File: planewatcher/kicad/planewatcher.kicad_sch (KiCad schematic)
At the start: 14 parts, among them J2 RF_IN, J3 BMI-S-209-F, J4 FPGA BANK 33, J5 FPGA BANK 35 V1.2/V1.3, J6 GPS _IN

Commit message: review & consolidate all capacitors
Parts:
- C1: Design Notes (none) -> ~18µF after DC bias de-rating; MPN CL31A226KOHNNNE -> GCJ31CR71A226KE01K; Manufacturer Samsung -> Murata Electronics; Package 1206 -> 1206 (3216 Metric); Suggested Part Samsung CL31A226KOHNNNE -> (none)
- C2: MPN GRM155R71H104KE14D -> GCM155R71A104KA55D; Manufacturer Murata -> Murata Electronics; Package 1206 -> 0402 (1005 Metric); Suggested Part Murata GRM155R71H104KE14D -> (none)
- C3: MPN GRM1555C1H102JA01D -> GRM1555C1H102FA01D; Manufacturer Murata -> Murata Electronics; Package 0402 -> 0402 (1005 Metric); Suggested Part Murata GRM1555C1H102JA01D -> (none)
- FL1, FL2: Suggested Part Tai-Saw TA2003A -> (none)
- J2: Suggested Part Amphenol RF 132289 -> (none)
- J3: Suggested Part Laird/BMI BMI-S-209-F -> (none)
- J4, J5: Suggested Part Samtec TSW-120-07-L-D -> (none)
- J6: Purpose Accepts the external 1090MHz antenna input. -> Accepts the external GPS/GNSS antenna input.; Suggested Part Amphenol RF 132289 -> (none)
- L1: Suggested Part Würth Elektronik 74269262601 -> (none)
- R1: Suggested Part Yageo RC0402FR-0710KL -> (none)
- R2: Suggested Part Yageo RC0402FR-07330RL -> (none)
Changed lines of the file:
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@@
 			)
 		)
-		(property "Suggested Part" "Samtec TSW-120-07-L-D"
+		(property "Purpose" "Breaks out FPGA bank 35 I/O and power pins to the carrier/FPGA interface."
 			(at 106.68 168.91 0)
 			(hide yes)
@@
 			)
 		)
-		(property "Purpose" "Breaks out FPGA bank 35 I/O and power pins to the carrier/FPGA interface."
+		(property "Notes" ""
 			(at 106.68 168.91 0)
 			(hide yes)
@@
 			)
 		)
-		(property "Notes" ""
+		(property "Mount_Type" ""
 			(at 106.68 168.91 0)
 			(hide yes)
@@
 			)
 		)
-		(property "Suggested Part" "Yageo RC0402FR-07330RL"
+		(property "Purpose" "Series resistor between LT3045 power-good output and the FPGA monitor input."
 			(at 184.15 36.83 0)
 			(hide yes)
@@
 			)
 		)
-		(property "Purpose" "Series resistor between LT3045 power-good output and the FPGA monitor input."
+		(property "Mount_Type" ""
 			(at 184.15 36.83 0)
 			(hide yes)
@@
 			)
 		)
-		(property "Datasheet" ""
+		(property "Datasheet" "https://pim.murata.com/en-sg/pim/details/?partNum=GCJ31CR71A226KE01%23&displayChangeClass=productDetailPrint"
 			(at 120.65 38.1 0)
 			(hide yes)
@@
 			)
 		)
-		(property "Description" "22µF, X5R, ±10%, 16V, 1206 MLCC"
+		(property "Description" "22 µF ±10% 10V Ceramic Capacitor X7R 1206 (3216 Metric)"
 			(at 120.65 38.1 0)
 			(hide yes)
@@
 			)
 		)
-		(property "Package" "1206"
+		(property "Package" "1206 (3216 Metric)"
 			(at 120.65 38.1 0)
 			(hide yes)
@@
 			)
 		)
-		(property "MPN" "CL31A226KOHNNNE"
+		(property "MPN" "GCJ31CR71A226KE01K"
 			(at 120.65 38.1 0)
 			(hide yes)
@@
 			)
 		)
-		(property "Manufacturer" "Samsung"
+		(property "Manufacturer" "Murata Electronics"
 			(at 120.65 38.1 0)
 			(hide yes)
@@
 			)
 		)
-		(property "Suggested Part" "Samsung CL31A226KOHNNNE"
+		(property "Purpose" "Load-side bulk decoupling for the filtered 3V3A analog rail."
 			(at 120.65 38.1 0)
 			(hide yes)
@@
 			)
 		)
-		(property "Purpose" "Load-side bulk decoupling for the filtered 3V3A analog rail."
+		(property "Design Notes" "~18µF after DC bias de-rating"
+			(at 120.65 38.1 0)
+			(hide yes)
+			(show_name no)
+			(do_not_autoplace no)
+			(effects
+				(font
+					(size 1.27 1.27)
+				)
+			)
+		)
+		(property "Mount_Type" ""
 			(at 120.65 38.1 0)
 			(hide yes)
@@
 			)
 		)
-		(property "Datasheet" ""
+		(property "Datasheet" "https://search.murata.co.jp/Ceramy/image/img/A01X/G101/ENG/GCM155R71A104KA55-01.pdf"
 			(at 133.35 38.1 0)
 			(hide yes)
@@
 			)
 		)
-		(property "Description" "100nF, X7R, ±10%, 50V, 0402 MLCC"
+		(property "Description" "0.1 µF ±10% 10V Ceramic Capacitor X7R 0402 (1005 Metric)"
 			(at 133.35 38.1 0)
 			(hide yes)
@@
 			)
 		)
-		(property "Package" "1206"
+		(property "Package" "0402 (1005 Metric)"
 			(at 133.35 38.1 0)
 			(hide yes)
@@
 			)
 		)
-		(property "MPN" "GRM155R71H104KE14D"
+		(property "MPN" "GCM155R71A104KA55D"
 			(at 133.35 38.1 0)
 			(hide yes)
@@
 			)
 		)
-		(property "Manufacturer" "Murata"
+		(property "Manufacturer" "Murata Electronics"
 			(at 133.35 38.1 0)
 			(hide yes)
@@
 			)
 		)
-		(property "Suggested Part" "Murata GRM155R71H104KE14D"
+		(property "Purpose" "Load-side high-frequency decoupling for the filtered 3V3A analog rail."
 			(at 133.35 38.1 0)
 			(hide yes)
@@
 			)
 		)
-		(property "Purpose" "Load-side high-frequency decoupling for the filtered 3V3A analog rail."
+		(property "Mount_Type" ""
 			(at 133.35 38.1 0)
 			(hide yes)
@@
 			)
 		)
-		(property "Suggested Part" "Yageo RC0402FR-0710KL"
+		(property "Purpose" "Pulls the LT3045 open-collector power-good output up to 3V3."
 			(at 184.15 29.21 0)
 			(hide yes)
@@
 			)
 		)
-		(property "Purpose" "Pulls the LT3045 open-collector power-good output up to 3V3."
+		(property "Mount_Type" ""
 			(at 184.15 29.21 0)
 			(hide yes)
@@
 			)
 		)
+		(property "Mount_Type" ""
+			(at 127 34.29 0)
+			(hide yes)
+			(show_name no)
+			(do_not_autoplace no)
+			(effects
+				(font
+					(size 1.27 1.27)
+				)
+			)
+		)
 		(pin "1"
 		)
@@
 			)
 		)
-		(property "Suggested Part" "Tai-Saw TA2003A"
+		(property "Purpose" "Band-limits the ADS-B 1090MHz RF path and rejects out-of-band energy."
 			(at 96.52 77.47 0)
 			(hide yes)
@@
 			)
 		)
-		(property "Purpose" "Band-limits the ADS-B 1090MHz RF path and rejects out-of-band energy."
+		(property "Notes" ""
 			(at 96.52 77.47 0)
 			(hide yes)
@@
 			)
 		)
-		(property "Notes" ""
+		(property "Mount_Type" ""
 			(at 96.52 77.47 0)
 			(hide yes)
@@
 			)
 		)
-		(property "Suggested Part" "Laird/BMI BMI-S-209-F"
+		(property "Purpose" "Shields the RF front-end area from external and board-level interference."
 			(at 179.07 100.33 0)
 			(hide yes)
@@
 			)
 		)
-		(property "Purpose" "Shields the RF front-end area from external and board-level interference."
+		(property "Mount_Type" ""
 			(at 179.07 100.33 0)
 			(hide yes)
@@
 			)
 		)
-		(property "Suggested Part" "Samtec TSW-120-07-L-D"
+		(property "Purpose" "Breaks out FPGA bank 33 I/O and power pins to the carrier/FPGA interface."
 			(at 45.72 168.91 0)
 			(hide yes)
@@
 			)
 		)
-		(property "Purpose" "Breaks out FPGA bank 33 I/O and power pins to the carrier/FPGA interface."
+		(property "Notes" ""
 			(at 45.72 168.91 0)
 			(hide yes)
@@
 			)
 		)
-		(property "Notes" ""
+		(property "Mount_Type" ""
 			(at 45.72 168.91 0)
 			(hide yes)
@@
 			)
 		)
-		(property "Suggested Part" "Tai-Saw TA2003A"
+		(property "Purpose" "Band-limits the ADS-B 1090MHz RF path and rejects out-of-band energy."
 			(at 149.86 77.47 0)
 			(hide yes)
@@
 			)
 		)
-		(property "Purpose" "Band-limits the ADS-B 1090MHz RF path and rejects out-of-band energy."
+		(property "Notes" ""
 			(at 149.86 77.47 0)
 			(hide yes)
@@
 			)
 		)
-		(property "Notes" ""
+		(property "Mount_Type" ""
 			(at 149.86 77.47 0)
 			(hide yes)
@@
 			)
 		)
-		(property "Datasheet" ""
+		(property "Datasheet" "https://search.murata.co.jp/Ceramy/image/img/A01X/G101/ENG/GRM1555C1H102FA01-01.pdf"
 			(at 146.05 38.1 0)
 			(hide yes)
@@
 			)
 		)
-		(property "Description" "1nF, C0G/NP0, ±5%, 50V, 0402 MLCC"
+		(property "Description" "1000 pF ±1% 50V Ceramic Capacitor C0G, NP0 0402 (1005 Metric)"
 			(at 146.05 38.1 0)
 			(hide yes)
@@
 			)
 		)
-		(property "Package" "0402"
+		(property "Package" "0402 (1005 Metric)"
 			(at 146.05 38.1 0)
 			(hide yes)
@@
 			)
 		)
-		(property "MPN" "GRM1555C1H102JA01D"
+		(property "MPN" "GRM1555C1H102FA01D"
 			(at 146.05 38.1 0)
 			(hide yes)
@@
 			)
 		)
-		(property "Manufacturer" "Murata"
+		(property "Manufacturer" "Murata Electronics"
 			(at 146.05 38.1 0)
 			(hide yes)
@@
 			)
 		)
-		(property "Suggested Part" "Murata GRM1555C1H102JA01D"
+		(property "Purpose" "Load-side RF decoupling for the filtered 3V3A analog rail."
 			(at 146.05 38.1 0)
 			(hide yes)
@@
 			)
 		)
-		(property "Purpose" "Load-side RF decoupling for the filtered 3V3A analog rail."
+		(property "Mount_Type" ""
 			(at 146.05 38.1 0)
 			(hide yes)
@@
 			)
 		)
-		(property "Suggested Part" "Amphenol RF 132289"
+		(property "Purpose" "Accepts the external 1090MHz antenna input."
 			(at 21.59 85.09 0)
 			(hide yes)
@@
 			)
 		)
-		(property "Purpose" "Accepts the external 1090MHz antenna input."
+		(property "Notes" ""
 			(at 21.59 85.09 0)
 			(hide yes)
@@
 			)
 		)
-		(property "Notes" ""
+		(property "Mount_Type" ""
 			(at 21.59 85.09 0)
 			(hide yes)
@@
 			)
 		)
-		(property "Suggested Part" "Würth Elektronik 74269262601"
+		(property "Purpose" "Ferrite bead isolation between the 3V3 regulator output and the 3V3A analog rail."
 			(at 109.22 34.29 90)
 			(hide yes)
@@
 			)
 		)
-		(property "Purpose" "Ferrite bead isolation between the 3V3 regulator output and the 3V3A analog rail."
+		(property "Mount_Type" ""
 			(at 109.22 34.29 90)
 			(hide yes)
@@
 			)
 		)
-		(property "Suggested Part" "Amphenol RF 132289"
+		(property "Purpose" "Accepts the external GPS/GNSS antenna input."
 			(at 217.17 29.21 0)
 			(hide yes)
@@
 			)
 		)
-		(property "Purpose" "Accepts the external 1090MHz antenna input."
+		(property "Notes" ""
 			(at 217.17 29.21 0)
 			(hide yes)
@@
 			)
 		)
-		(property "Notes" ""
+		(property "Mount_Type" ""
 			(at 217.17 29.21 0)
 			(hide yes)

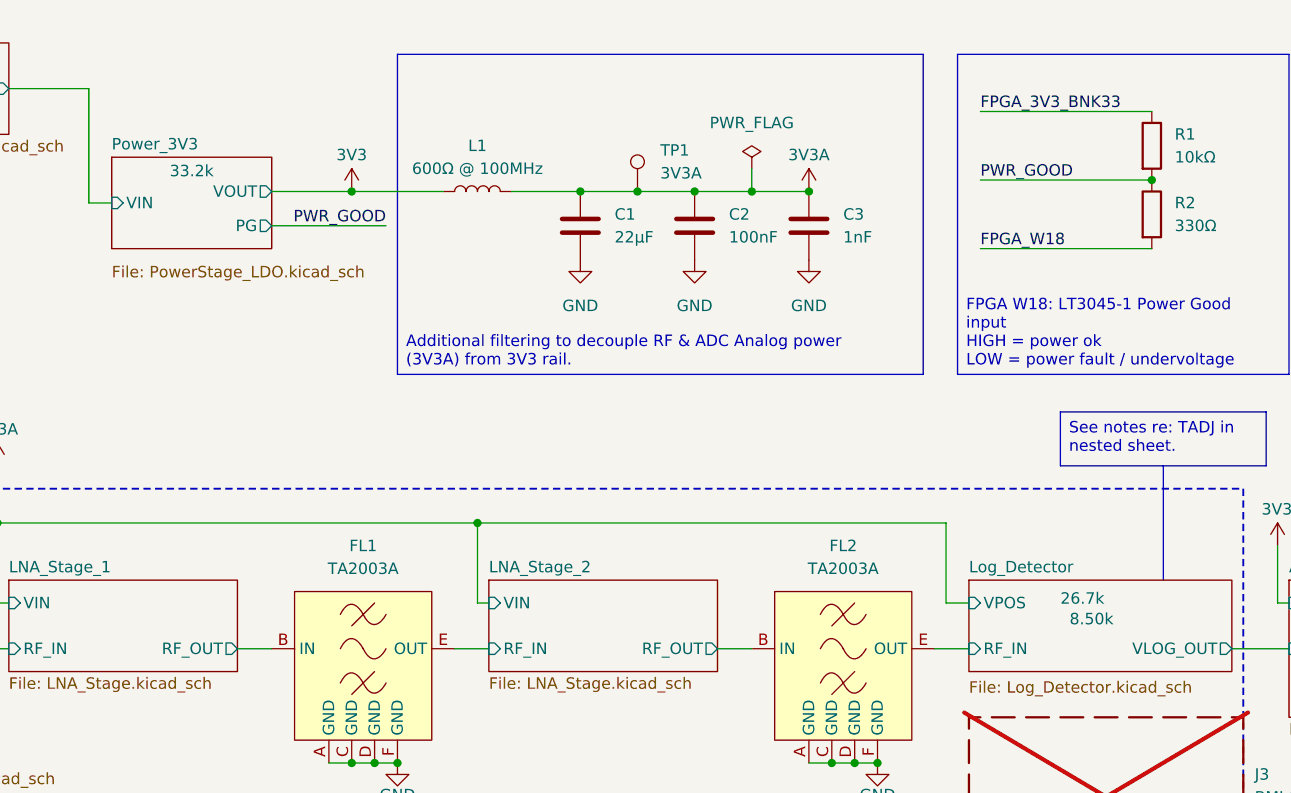
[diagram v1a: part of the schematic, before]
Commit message: review & consolidate all resistors
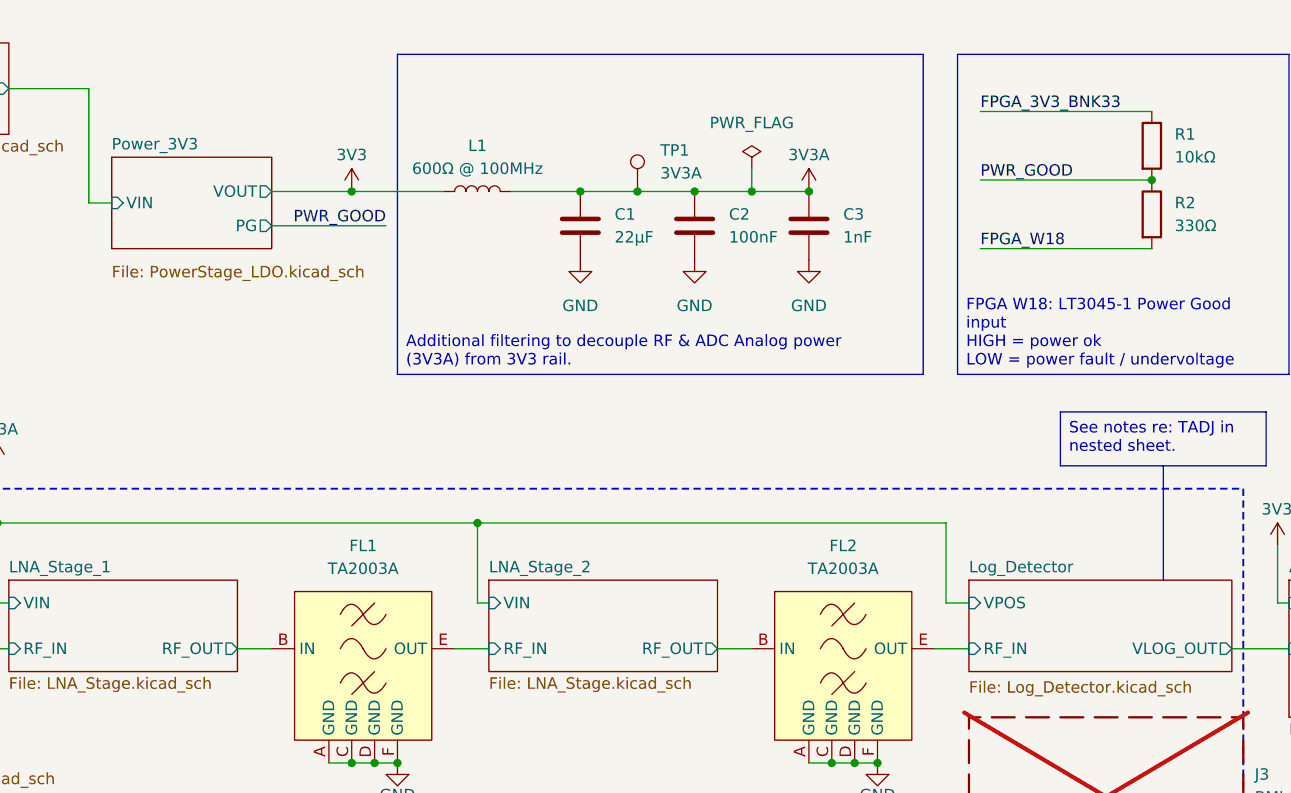
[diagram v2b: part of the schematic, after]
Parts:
- R1: MPN RC0402FR-0710KL -> RT0402FRE1310KL; Manufacturer Yageo -> YAGEO; Package 0402 -> 0402 (1005 Metric)
- R2: MPN RC0402FR-07330RL -> RT0402FRE07330RL; Manufacturer Yageo -> YAGEO; Package 0402 -> 0402 (1005 Metric)
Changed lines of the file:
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@@
 			)
 		)
-		(property "Datasheet" "https://www.yageogroup.com/component-documentation/download/specsheet/RC0402FR-07330RL"
+		(property "Datasheet" "https://yageogroup.com/content/datasheet/asset/file/PYU-RT_1-TO-0-01_ROHS_L"
 			(at 184.15 36.83 0)
 			(hide yes)
@@
 			)
 		)
-		(property "Description" "330Ω, ±1%, thick film, 100ppm/°C, 0402 chip resistor"
+		(property "Description" "330 Ohms ±1% 0.063W, 1/16W Chip Resistor 0402 (1005 Metric) Thin Film"
 			(at 184.15 36.83 0)
 			(hide yes)
@@
 			)
 		)
-		(property "Package" "0402"
+		(property "Package" "0402 (1005 Metric)"
 			(at 184.15 36.83 0)
 			(hide yes)
@@
 			)
 		)
-		(property "MPN" "RC0402FR-07330RL"
+		(property "MPN" "RT0402FRE07330RL"
 			(at 184.15 36.83 0)
 			(hide yes)
@@
 			)
 		)
-		(property "Manufacturer" "Yageo"
+		(property "Manufacturer" "YAGEO"
 			(at 184.15 36.83 0)
 			(hide yes)
@@
 			)
 		)
-		(property "Mount_Type" ""
-			(at 184.15 36.83 0)
-			(hide yes)
-			(show_name no)
-			(do_not_autoplace no)
-			(effects
-				(font
-					(size 1.27 1.27)
-				)
-			)
-		)
 		(pin "1"
 		)
@@
 			)
 		)
-		(property "Description" "10kΩ, ±1%, thick film, 100ppm/°C, 0402 chip resistor"
+		(property "Description" "10 kOhms ±1% 0.063W, 1/16W Chip Resistor 0402 (1005 Metric) Moisture Resistant Thin Film"
 			(at 184.15 29.21 0)
 			(hide yes)
@@
 			)
 		)
-		(property "Package" "0402"
+		(property "Package" "0402 (1005 Metric)"
 			(at 184.15 29.21 0)
 			(hide yes)
@@
 			)
 		)
-		(property "MPN" "RC0402FR-0710KL"
+		(property "MPN" "RT0402FRE1310KL"
 			(at 184.15 29.21 0)
 			(hide yes)
@@
 			)
 		)
-		(property "Manufacturer" "Yageo"
+		(property "Manufacturer" "YAGEO"
 			(at 184.15 29.21 0)
 			(hide yes)
@@
 			)
 		)
-		(property "Mount_Type" ""
-			(at 184.15 29.21 0)
-			(hide yes)
-			(show_name no)
-			(do_not_autoplace no)
-			(effects
-				(font
-					(size 1.27 1.27)
-				)
-			)
-		)
 		(pin "1"
 		)
@@
 			)
 		)
-		(property "RTADJ_VPOS" "26.7k"
-			(at 173.99 79.502 0)
-			(show_name yes)
-			(do_not_autoplace no)
-			(effects
-				(font
-					(size 1.27 1.27)
-				)
-				(justify left)
-			)
-		)
-		(property "RTADJ_GND" "8.50k"
-			(at 175.006 81.788 0)
-			(show_name yes)
-			(do_not_autoplace no)
-			(effects
-				(font
-					(size 1.27 1.27)
-				)
-				(justify left)
-			)
-		)
-		(property "RTADJ_VPOS_Suggested_Part" "Panasonic ERA-2AEB2672X"
-			(at 163.83 76.7584 0)
-			(hide yes)
-			(show_name no)
-			(do_not_autoplace no)
-			(effects
-				(font
-					(size 1.27 1.27)
-				)
-			)
-		)
-		(property "RTADJ_GND_Suggested_Part" "Panasonic ERA-2AEB8501X"
-			(at 163.83 76.7584 0)
-			(hide yes)
-			(show_name no)
-			(do_not_autoplace no)
-			(effects
-				(font
-					(size 1.27 1.27)
-				)
-			)
-		)
 		(pin "RF_IN" input
 			(at 163.83 85.09 180)
@@
 			)
 		)
-		(property "RSET" "33.2k"
-			(at 77.47 32.004 0)
-			(show_name yes)
-			(do_not_autoplace no)
-			(effects
-				(font
-					(size 1.27 1.27)
-				)
-			)
-		)
-		(property "RSET_Description" "33.2kΩ, ±0.1%, thin film, ≤25ppm/°C, 0603, LT3045 SET resistor (VOUT ≈ 100µA × RSET), Panasonic ERA-3AEB3322V"
-			(at 68.58 30.48 0)
-			(hide yes)
-			(show_name no)
-			(do_not_autoplace no)
-			(effects
-				(font
-					(size 1.27 1.27)
-				)
-			)
-		)
-		(property "RSET_Suggested_Part" "Panasonic ERA-3AEB3322V"
-			(at 68.58 30.48 0)
-			(hide yes)
-			(show_name no)
-			(do_not_autoplace no)
-			(effects
-				(font
-					(size 1.27 1.27)
-				)
-			)
-		)

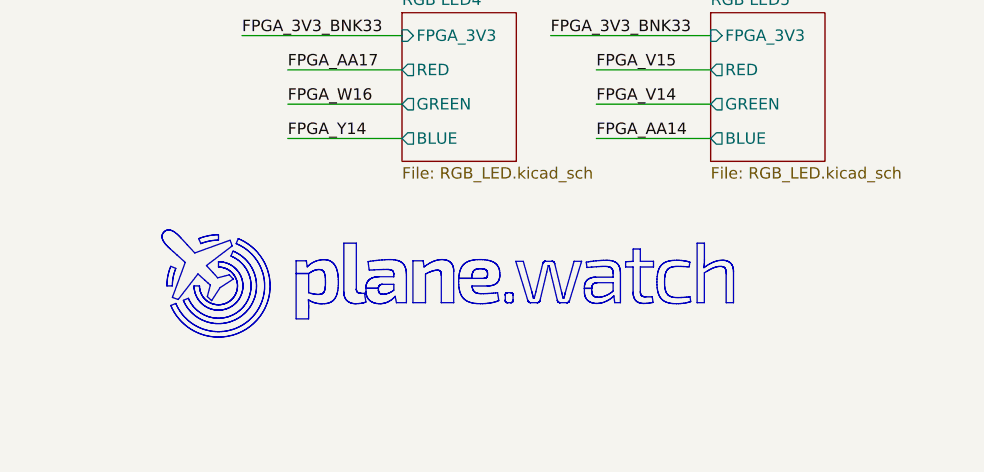
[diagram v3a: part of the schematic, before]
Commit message: add license & copyright info to schematic and pcb. fix layer window.
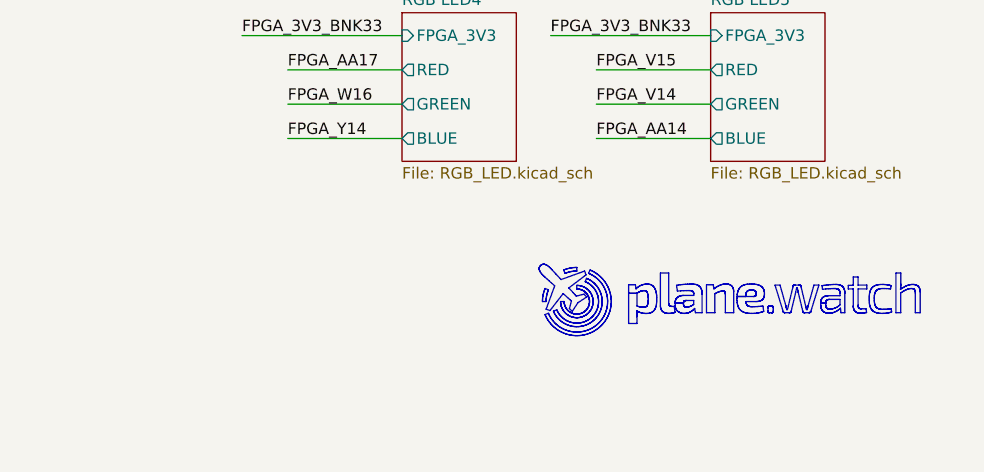
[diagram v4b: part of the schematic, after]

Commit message: added lcsc_ids to all parts
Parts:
- C1: lcsc_id (none) -> C3883047
- C2: lcsc_id (none) -> C161163
- C3: lcsc_id (none) -> C161523
- J2, J6: lcsc_id (none) -> C3172723
- J4, J5: lcsc_id (none) -> C5968215
- L1: lcsc_id (none) -> C5914022
- R1: lcsc_id (none) -> C5455557
- R2: lcsc_id (none) -> C854274
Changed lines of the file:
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@@
 	(polyline
 		(pts
-			(xy 242.3253 175.57) (xy 242.3253 175.57)
-		)
-		(stroke
-			(width -0.0001)
-			(type solid)
-		)
-		(fill
-			(type color)
-			(color 211 209 209 1)
-		)
-	)
-	(polyline
-		(pts
 			(xy 281.4795 174.9174) (xy 281.4789 175.0015) (xy 281.4772 175.0835) (xy 281.4742 175.1631) (xy 281.4701 175.2401)
 			(xy 281.4648 175.3142) (xy 281.4583 175.385) (xy 281.4506 175.4523) (xy 281.4417 175.5157) (xy 281.5278 175.4535)
@@
 		)
 	)
+	(polyline
+		(pts
+			(xy 242.3253 175.57) (xy 242.3253 175.57)
+		)
+		(stroke
+			(width -0.0001)
+			(type solid)
+		)
+	)
 	(wire
 		(pts
@@
 			)
 		)
+		(property "lcsc_id" "C5968215"
+			(at 106.68 168.91 0)
+			(hide yes)
+			(show_name no)
+			(do_not_autoplace no)
+			(effects
+				(font
+					(size 1.27 1.27)
+				)
+			)
+		)
 		(pin "23"
 		)
@@
 			)
 		)
+		(property "lcsc_id" "C854274"
+			(at 184.15 36.83 0)
+			(hide yes)
+			(show_name no)
+			(do_not_autoplace no)
+			(effects
+				(font
+					(size 1.27 1.27)
+				)
+			)
+		)
 		(pin "1"
 		)
@@
 			)
 		)
+		(property "lcsc_id" "C3883047"
+			(at 120.65 38.1 0)
+			(hide yes)
+			(show_name no)
+			(do_not_autoplace no)
+			(effects
+				(font
+					(size 1.27 1.27)
+				)
+			)
+		)
 		(pin "2"
 		)
@@
 			)
 		)
+		(property "lcsc_id" "C161163"
+			(at 133.35 38.1 0)
+			(hide yes)
+			(show_name no)
+			(do_not_autoplace no)
+			(effects
+				(font
+					(size 1.27 1.27)
+				)
+			)
+		)
 		(pin "2"
 		)
@@
 			)
 		)
+		(property "lcsc_id" "C5455557"
+			(at 184.15 29.21 0)
+			(hide yes)
+			(show_name no)
+			(do_not_autoplace no)
+			(effects
+				(font
+					(size 1.27 1.27)
+				)
+			)
+		)
 		(pin "1"
 		)
@@
 			)
 		)
+		(property "lcsc_id" "C5968215"
+			(at 45.72 168.91 0)
+			(hide yes)
+			(show_name no)
+			(do_not_autoplace no)
+			(effects
+				(font
+					(size 1.27 1.27)
+				)
+			)
+		)
 		(pin "23"
 		)
@@
 			)
 		)
+		(property "lcsc_id" "C161523"
+			(at 146.05 38.1 0)
+			(hide yes)
+			(show_name no)
+			(do_not_autoplace no)
+			(effects
+				(font
+					(size 1.27 1.27)
+				)
+			)
+		)
 		(pin "2"
 		)
@@
 			)
 		)
+		(property "lcsc_id" "C3172723"
+			(at 21.59 85.09 0)
+			(hide yes)
+			(show_name no)
+			(do_not_autoplace no)
+			(effects
+				(font
+					(size 1.27 1.27)
+				)
+			)
+		)
 		(pin "1"
 		)
@@
 			)
 		)
+		(property "lcsc_id" "C5914022"
+			(at 109.22 34.29 0)
+			(hide yes)
+			(show_name no)
+			(do_not_autoplace no)
+			(effects
+				(font
+					(size 1.27 1.27)
+				)
+			)
+		)
 		(pin "2"
 		)
@@
 			(at 217.17 29.21 0)
 			(hide yes)
+			(show_name no)
+			(do_not_autoplace no)
+			(effects
+				(font
+					(size 1.27 1.27)
+				)
+			)
+		)
+		(property "lcsc_id" "C3172723"
+			(at 217.17 29.21 0)
+			(hide yes)
